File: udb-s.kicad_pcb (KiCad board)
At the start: 4 copper layers, 40 x 9 mm, 9 parts, among them J1 TYPE-C-31-M-12, J2 SM04B-SRSS, U2 USBLC6-2SC6

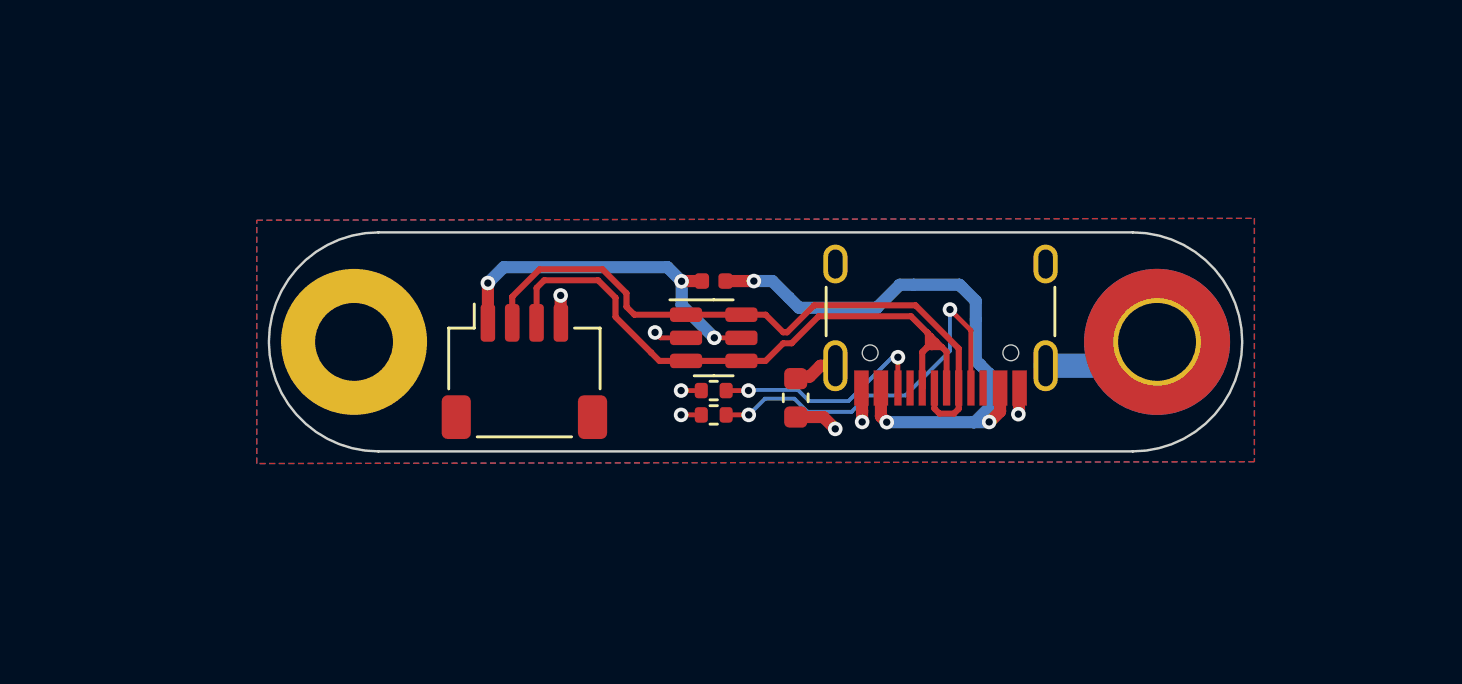
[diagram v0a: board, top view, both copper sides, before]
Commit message: changed the layout so it can be assembled by jlc :)
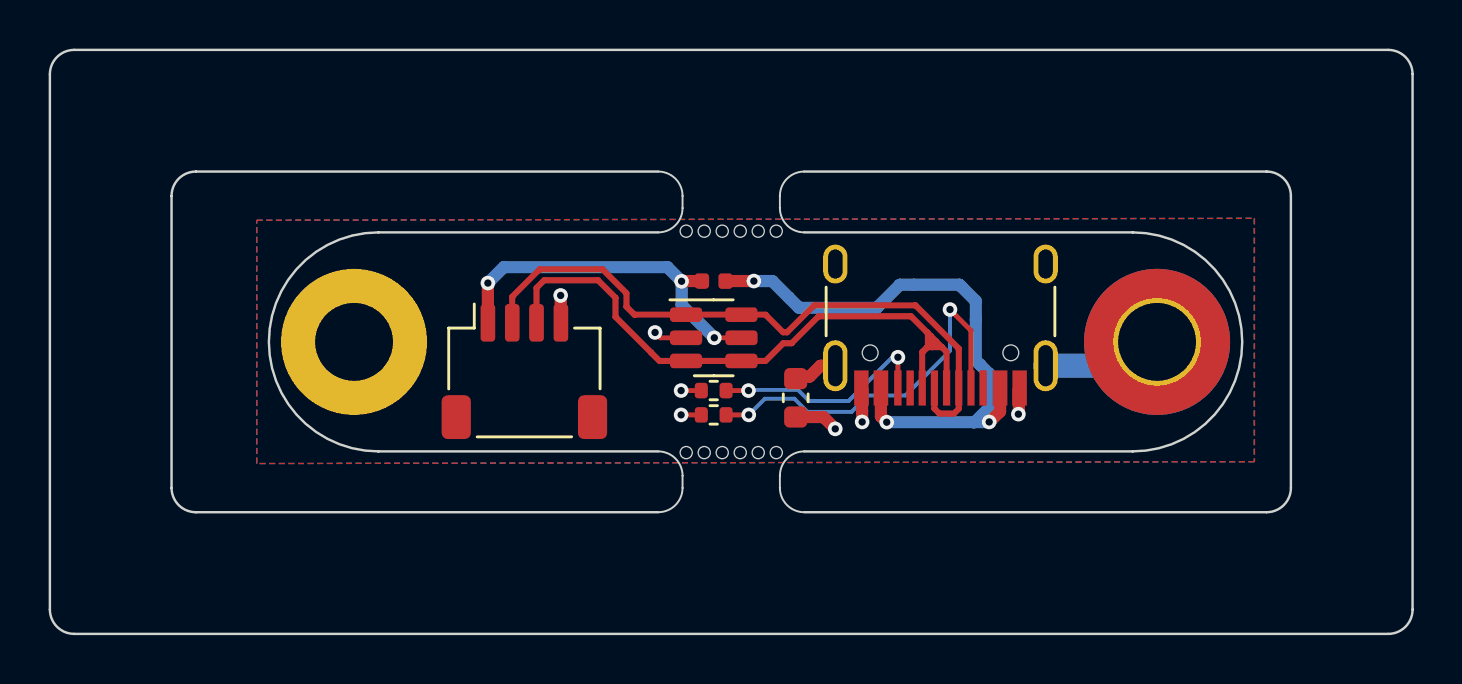
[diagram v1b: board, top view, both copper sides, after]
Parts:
- added REF**: mousebites 2mm, PCM_marbastlib-various:mousebites_2.5mm, F.Cu at (130.5, 90.5)
- added REF**: mousebites 2mm, PCM_marbastlib-various:mousebites_2.5mm, F.Cu at (130.5, 99.5)
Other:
- board size 40 x 9 mm -> 56 x 24 mm
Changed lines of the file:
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@@
     (pad_to_mask_clearance 0)
     (aux_axis_origin 115 95)
-    (grid_origin 115 95)
+    (grid_origin 111.499999 95)
     (pcbplotparams
       (layerselection 0x00010fc_ffffffff)
@@
     )
   )
+  (footprint "PCM_marbastlib-various:mousebites_2.5mm" (layer "F.Cu")
+    (at 130.499996 90.500003 -90)
+    (attr exclude_from_pos_files exclude_from_bom)
+    (fp_text reference "REF**" (at -4 -2.75 90) (layer "F.SilkS") hide
+        (effects (font (size 1 1) (thickness 0.15)))
+    )
+    (fp_text value "mousebites 2mm" (at 0.25 -1.5 90) (layer "F.Fab") hide
+        (effects (font (size 1 1) (thickness 0.15)))
+    )
+    (fp_line (start -1.5 -2) (end -1 -2)
+      (stroke (width 0.08) (type solid)) (layer "Edge.Cuts"))
+    (fp_line (start -1 2) (end -1.5 2)
+      (stroke (width 0.08) (type solid)) (layer "Edge.Cuts"))
+    (fp_arc (start -2.5 3) (mid -2.207108 2.292895) (end -1.500003 2.000003)
+      (stroke (width 0.08) (type solid)) (layer "Edge.Cuts"))
+    (fp_arc (start -1.5 -2) (mid -2.207105 -2.292892) (end -2.499997 -2.999997)
+      (stroke (width 0.08) (type solid)) (layer "Edge.Cuts"))
+    (fp_arc (start -1 2) (mid -0.292895 2.292892) (end -0.000003 2.999997)
+      (stroke (width 0.08) (type solid)) (layer "Edge.Cuts"))
+    (fp_arc (start 0 -3) (mid -0.292892 -2.292895) (end -0.999997 -2.000003)
+      (stroke (width 0.08) (type solid)) (layer "Edge.Cuts"))
+    (pad "" np_thru_hole circle (at -0.05 -1.85 270) (size 0.5 0.5) (drill 0.5) (layers "F&B.Cu" "*.Mask"))
+    (pad "" np_thru_hole circle (at -0.05 -1.11 270) (size 0.5 0.5) (drill 0.5) (layers "F&B.Cu" "*.Mask"))
+    (pad "" np_thru_hole circle (at -0.05 -0.37 270) (size 0.5 0.5) (drill 0.5) (layers "F&B.Cu" "*.Mask"))
+    (pad "" np_thru_hole circle (at -0.05 0.37 270) (size 0.5 0.5) (drill 0.5) (layers "F&B.Cu" "*.Mask"))
+    (pad "" np_thru_hole circle (at -0.05 1.11 270) (size 0.5 0.5) (drill 0.5) (layers "F&B.Cu" "*.Mask"))
+    (pad "" np_thru_hole circle (at -0.05 1.85 270) (size 0.5 0.5) (drill 0.5) (layers "F&B.Cu" "*.Mask"))
+  )
   (footprint "Package_TO_SOT_SMD:SOT-23-6" (layer "F.Cu")
     (at 129.779999 94.832207)
@@
       (rotate (xyz 0 0 0))
     )
+  )
+  (footprint "PCM_marbastlib-various:mousebites_2.5mm" (layer "F.Cu")
+    (at 130.499999 99.5 90)
+    (attr exclude_from_pos_files exclude_from_bom)
+    (fp_text reference "REF**" (at -4 -2.75 90) (layer "F.SilkS") hide
+        (effects (font (size 1 1) (thickness 0.15)))
+    )
+    (fp_text value "mousebites 2mm" (at 0.25 -1.5 90) (layer "F.Fab") hide
+        (effects (font (size 1 1) (thickness 0.15)))
+    )
+    (fp_line (start -1.5 -2) (end -1 -2)
+      (stroke (width 0.08) (type solid)) (layer "Edge.Cuts"))
+    (fp_line (start -1 2) (end -1.5 2)
+      (stroke (width 0.08) (type solid)) (layer "Edge.Cuts"))
+    (fp_arc (start -2.5 3) (mid -2.207108 2.292895) (end -1.500003 2.000003)
+      (stroke (width 0.08) (type solid)) (layer "Edge.Cuts"))
+    (fp_arc (start -1.5 -2) (mid -2.207105 -2.292892) (end -2.499997 -2.999997)
+      (stroke (width 0.08) (type solid)) (layer "Edge.Cuts"))
+    (fp_arc (start -1 2) (mid -0.292895 2.292892) (end -0.000003 2.999997)
+      (stroke (width 0.08) (type solid)) (layer "Edge.Cuts"))
+    (fp_arc (start 0 -3) (mid -0.292892 -2.292895) (end -0.999997 -2.000003)
+      (stroke (width 0.08) (type solid)) (layer "Edge.Cuts"))
+    (pad "" np_thru_hole circle (at -0.05 -1.85 90) (size 0.5 0.5) (drill 0.5) (layers "F&B.Cu" "*.Mask"))
+    (pad "" np_thru_hole circle (at -0.05 -1.11 90) (size 0.5 0.5) (drill 0.5) (layers "F&B.Cu" "*.Mask"))
+    (pad "" np_thru_hole circle (at -0.05 -0.37 90) (size 0.5 0.5) (drill 0.5) (layers "F&B.Cu" "*.Mask"))
+    (pad "" np_thru_hole circle (at -0.05 0.37 90) (size 0.5 0.5) (drill 0.5) (layers "F&B.Cu" "*.Mask"))
+    (pad "" np_thru_hole circle (at -0.05 1.11 90) (size 0.5 0.5) (drill 0.5) (layers "F&B.Cu" "*.Mask"))
+    (pad "" np_thru_hole circle (at -0.05 1.85 90) (size 0.5 0.5) (drill 0.5) (layers "F&B.Cu" "*.Mask"))
   )
   (footprint "Resistor_SMD:R_0402_1005Metric" (layer "F.Cu")
@@
     )
   )
+  (gr_line (start 153.499999 101) (end 153.499999 89)
+    (stroke (width 0.1) (type default)) (layer "Edge.Cuts"))
+  (gr_arc (start 158.499999 106) (mid 158.207106 106.707107) (end 157.499999 107)
+    (stroke (width 0.1) (type default)) (layer "Edge.Cuts"))
+  (gr_line (start 152.499999 88) (end 133.499993 88.000006)
+    (stroke (width 0.1) (type default)) (layer "Edge.Cuts"))
+  (gr_line (start 133.499999 102) (end 152.499999 102)
+    (stroke (width 0.1) (type default)) (layer "Edge.Cuts"))
+  (gr_arc (start 157.499999 83) (mid 158.207106 83.292893) (end 158.499999 84)
+    (stroke (width 0.1) (type default)) (layer "Edge.Cuts"))
+  (gr_line (start 127.499996 88.000003) (end 108.499996 88.000003)
+    (stroke (width 0.1) (type default)) (layer "Edge.Cuts"))
   (gr_arc (start 116 99.500001) (mid 111.499999 95) (end 116 90.499999)
     (stroke (width 0.1) (type solid)) (layer "Edge.Cuts"))
+  (gr_line (start 116 99.500001) (end 127.499999 99.5)
+    (stroke (width 0.1) (type default)) (layer "Edge.Cuts"))
   (gr_arc (start 147 90.5) (mid 151.5 95) (end 147 99.5)
     (stroke (width 0.1) (type solid)) (layer "Edge.Cuts"))
-  (gr_line (start 147 90.5) (end 116 90.499999)
+  (gr_line (start 127.499999 90.5) (end 116 90.499999)
     (stroke (width 0.1) (type solid)) (layer "Edge.Cuts"))
-  (gr_line (start 116 99.500001) (end 147 99.5)
-    (stroke (width 0.1) (type solid)) (layer "Edge.Cuts"))
+  (gr_line (start 147 90.5) (end 133.499996 90.500003)
+    (stroke (width 0.1) (type default)) (layer "Edge.Cuts"))
+  (gr_line (start 158.499999 84) (end 158.499999 106)
+    (stroke (width 0.1) (type default)) (layer "Edge.Cuts"))
+  (gr_line (start 103.499999 83) (end 157.499999 83)
+    (stroke (width 0.1) (type default)) (layer "Edge.Cuts"))
+  (gr_line (start 107.499996 89.000003) (end 107.499996 101.000003)
+    (stroke (width 0.1) (type default)) (layer "Edge.Cuts"))
+  (gr_line (start 102.499999 106) (end 102.499999 84)
+    (stroke (width 0.1) (type default)) (layer "Edge.Cuts"))
+  (gr_line (start 157.499999 107) (end 103.499999 107)
+    (stroke (width 0.1) (type default)) (layer "Edge.Cuts"))
+  (gr_arc (start 102.499999 84) (mid 102.792892 83.292893) (end 103.499999 83)
+    (stroke (width 0.1) (type default)) (layer "Edge.Cuts"))
+  (gr_arc (start 108.499996 102.000003) (mid 107.792889 101.70711) (end 107.499996 101.000003)
+    (stroke (width 0.1) (type default)) (layer "Edge.Cuts"))
+  (gr_arc (start 153.499999 101) (mid 153.207106 101.707107) (end 152.499999 102)
+    (stroke (width 0.1) (type default)) (layer "Edge.Cuts"))
+  (gr_arc (start 103.499999 107) (mid 102.792892 106.707107) (end 102.499999 106)
+    (stroke (width 0.1) (type default)) (layer "Edge.Cuts"))
+  (gr_line (start 108.499996 102.000003) (end 127.500002 101.999997)
+    (stroke (width 0.1) (type default)) (layer "Edge.Cuts"))
+  (gr_arc (start 152.499999 88) (mid 153.207106 88.292893) (end 153.499999 89)
+    (stroke (width 0.1) (type default)) (layer "Edge.Cuts"))
+  (gr_line (start 133.499996 99.500003) (end 147 99.5)
+    (stroke (width 0.1) (type default)) (layer "Edge.Cuts"))
+  (gr_arc (start 107.499996 89.000003) (mid 107.792888 88.292893) (end 108.499996 88.000003)
+    (stroke (width 0.1) (type default)) (layer "Edge.Cuts"))
   (gr_text "hunger solving\nworld peace giving\nuniversal son board\n" (at 123 95) (layer "B.Mask")
     (effects (font (face "FreeSans") (size 0.5 0.5) (thickness 0.125)) (justify mirror))

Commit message: Adjusted ferrite bead location and changed mousebites
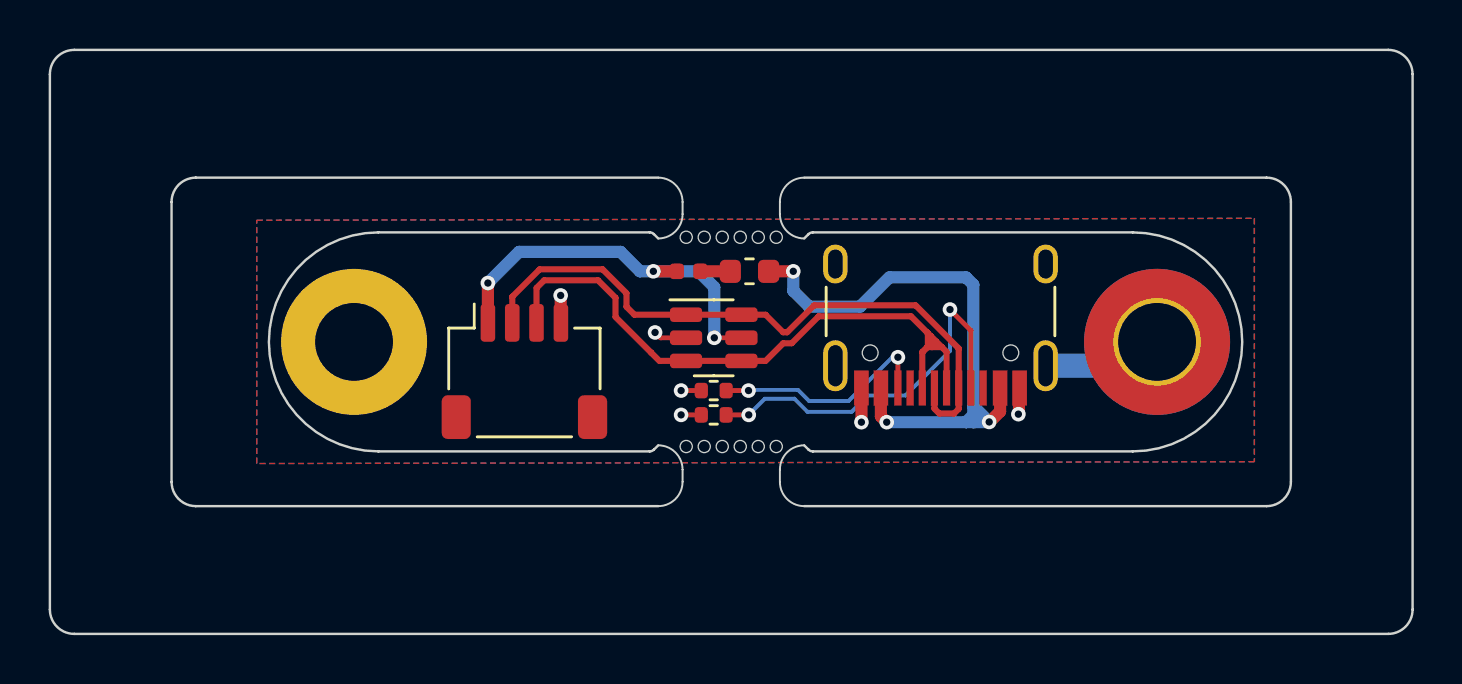
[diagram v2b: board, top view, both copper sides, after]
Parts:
- removed F2: 1A PTC, Fuse:Fuse_0402_1005Metric
- removed the REF** at (130.5, 90.5)
- removed the REF** at (130.5, 99.5)
- added F1: 1A PTC, Fuse:Fuse_0402_1005Metric, F.Cu at (128.7, 92.1)
- added REF**: mousebites 2mm, marbastlib-various:mousebites_2.5mm, F.Cu at (130.5, 99.2)
- added REF**: mousebites 2mm, marbastlib-various:mousebites_2.5mm, F.Cu at (130.5, 90.8)
- moved FB1 5.54 mm to (131.2, 92.1), turned to 180 degrees
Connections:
- FB1 pad 1: GNDPWR -> VBUS
- FB1 pad 2: GND -> Net-(F1-Pad1)
- H1 pad 1: GNDPWR -> GND
- J1 pad S1: GNDPWR -> GND
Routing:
- net GNDPWR: track 6.88 -> 0.00 mm
- net GND: track 8.44 -> 11.6 mm, vias 7 -> 6
- net 5V: track 14.9 -> 16.2 mm
- net Net-(F1-Pad1): track 0.00 -> 1.23 mm
- net VBUS: track 24.8 -> 24.2 mm
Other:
- outline, holes or cut-outs redrawn
